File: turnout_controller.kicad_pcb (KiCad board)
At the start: 2 copper layers, 25.4 x 12.7 mm, 31 parts, among them J1 DCC_A, J2 DCC_B, J3 PROG, J4 MOT_CNTL, J5 MOT_POWER, J6 MOT_GND, J7 LED_1, J8 LED_2, SW1 SW_Push, SW2 SW_Push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

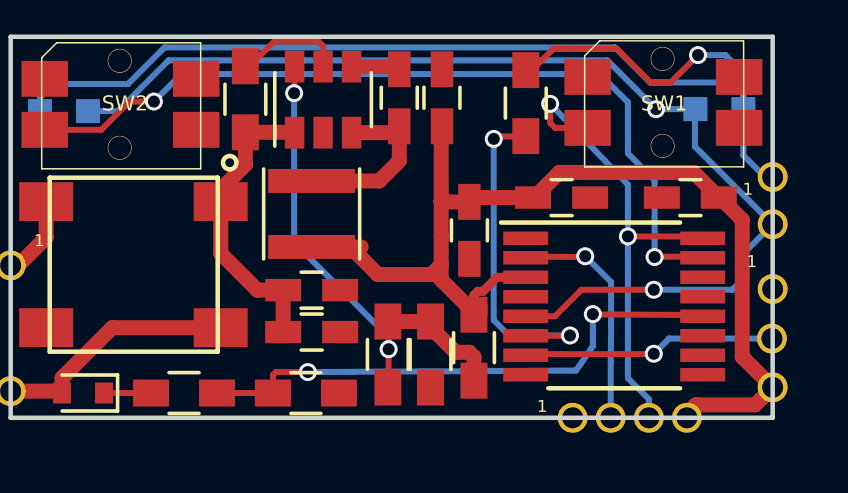
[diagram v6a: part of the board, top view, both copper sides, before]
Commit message: DRC fixes (via moved, trace modified. No GND connections.
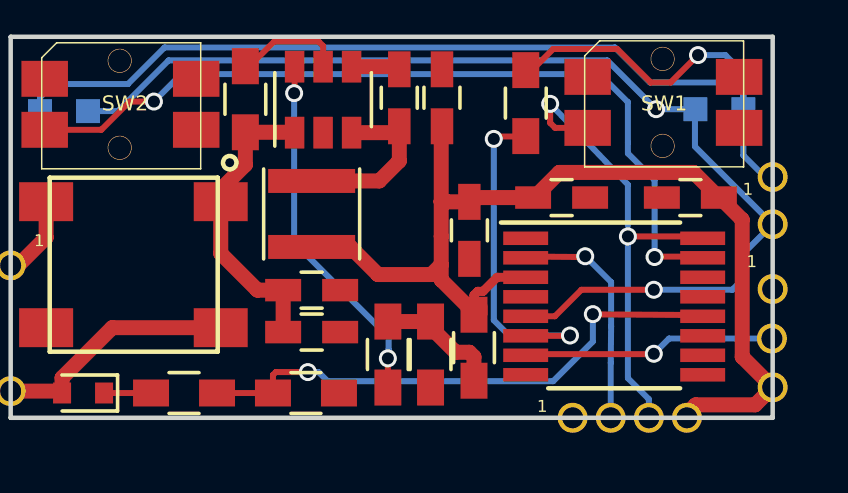
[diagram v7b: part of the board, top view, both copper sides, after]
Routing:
- net 5V: track 37.9 -> 36.3 mm
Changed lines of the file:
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@@
     (thickness 1.6)
     (drawings 10)
-    (tracks 189)
+    (tracks 192)
     (zones 0)
     (modules 31)
@@
   )
   (setup
-    (last_trace_width 0.5)
+    (last_trace_width 0.2)
     (user_trace_width 0.2)
     (user_trace_width 0.3)
@@
   (segment (start 154.1272 81.5848) (end 153.035 80.4926) (width 0.5) (layer F.Cu) (net 5))
   (segment (start 153.035 80.4926) (end 153.035 79.9846) (width 0.5) (layer F.Cu) (net 5))
-  (segment (start 148.717 79.3955) (end 150.368 79.3955) (width 0.5) (layer F.Cu) (net 5))
   (segment (start 148.717 79.3955) (end 150.0075 79.3955) (width 0.5) (layer F.Cu) (net 5))
   (segment (start 150.0075 79.3955) (end 150.9268 80.3148) (width 0.5) (layer F.Cu) (net 5))
@@
   (segment (start 148.9456 72.5424) (end 149.098 72.6948) (width 0.2) (layer F.Cu) (net 11))
   (segment (start 149.098 72.6948) (end 149.098 73.3855) (width 0.2) (layer F.Cu) (net 11))
+  (segment (start 148.59 83.566) (end 148.9456 83.566) (width 0.2) (layer B.Cu) (net 12))
+  (segment (start 147.4265 83.6627) (end 147.5232 83.566) (width 0.2) (layer F.Cu) (net 12))
+  (segment (start 147.5232 83.566) (end 148.59 83.566) (width 0.2) (layer F.Cu) (net 12))
+  (via (at 148.59 83.566) (size 0.6) (drill 0.4) (layers F.Cu B.Cu) (net 12))
   (segment (start 147.4265 84.2645) (end 147.4265 83.6627) (width 0.2) (layer F.Cu) (net 12))
-  (segment (start 157.5308 83.5152) (end 158.0896 82.7024) (width 0.2) (layer B.Cu) (net 12))
-  (segment (start 158.0896 82.7024) (end 158.0896 81.6356) (width 0.2) (layer B.Cu) (net 12))
-  (via (at 148.59 83.566) (size 0.6) (drill 0.4) (layers F.Cu B.Cu) (net 12))
+  (segment (start 156.7688 83.8708) (end 158.0896 82.55) (width 0.2) (layer B.Cu) (net 12))
+  (segment (start 149.2504 83.8708) (end 156.7688 83.8708) (width 0.2) (layer B.Cu) (net 12))
+  (segment (start 148.9456 83.566) (end 149.2504 83.8708) (width 0.2) (layer B.Cu) (net 12))
+  (segment (start 158.0896 82.55) (end 158.0896 81.6356) (width 0.2) (layer B.Cu) (net 12))
+  (segment (start 158.0971 81.6431) (end 162.1445 81.6685) (width 0.2) (layer F.Cu) (net 12))
+  (segment (start 158.0896 81.6356) (end 158.0971 81.6431) (width 0.2) (layer F.Cu) (net 12))
   (via (at 158.0896 81.6356) (size 0.6) (drill 0.4) (layers F.Cu B.Cu) (net 12))
-  (segment (start 158.0896 81.6356) (end 158.0971 81.6431) (width 0.2) (layer F.Cu) (net 12))
-  (segment (start 158.0971 81.6431) (end 162.1445 81.6685) (width 0.2) (layer F.Cu) (net 12))
-  (segment (start 148.59 83.566) (end 157.5308 83.5152) (width 0.2) (layer B.Cu) (net 12))
-  (segment (start 147.5232 83.566) (end 148.59 83.566) (width 0.2) (layer F.Cu) (net 12))
-  (segment (start 147.4265 83.6627) (end 147.5232 83.566) (width 0.2) (layer F.Cu) (net 12))
   (segment (start 145.5625 84.2645) (end 147.4265 84.2645) (width 0.2) (layer F.Cu) (net 12))
+  (segment (start 151.257 84.0818) (end 151.257 83.1088) (width 0.2) (layer F.Cu) (net 13))
+  (segment (start 151.2824 82.3976) (end 148.1328 79.248) (width 0.2) (layer B.Cu) (net 13))
+  (segment (start 148.1328 79.248) (end 148.1328 74.2696) (width 0.2) (layer B.Cu) (net 13))
   (segment (start 151.2824 82.804) (end 151.2824 82.3976) (width 0.2) (layer B.Cu) (net 13))
-  (via (at 151.2824 82.804) (size 0.6) (drill 0.4) (layers F.Cu B.Cu) (net 13))
-  (segment (start 151.2824 83.8532) (end 151.2824 82.804) (width 0.2) (layer F.Cu) (net 13))
-  (segment (start 148.1328 79.248) (end 148.1328 74.2696) (width 0.2) (layer B.Cu) (net 13))
-  (segment (start 151.2824 82.3976) (end 148.1328 79.248) (width 0.2) (layer B.Cu) (net 13))
+  (segment (start 151.2824 83.0834) (end 151.2824 82.804) (width 0.2) (layer B.Cu) (net 13))
+  (segment (start 151.257 83.1088) (end 151.2824 83.0834) (width 0.2) (layer B.Cu) (net 13))
+  (via (at 151.257 83.1088) (size 0.6) (drill 0.4) (layers F.Cu B.Cu) (net 13))
   (segment (start 148.1328 74.4728) (end 148.1328 74.2696) (width 0.2) (layer B.Cu) (net 13))
   (segment (start 148.148 74.2544) (end 148.148 73.3855) (width 0.2) (layer F.Cu) (net 13))

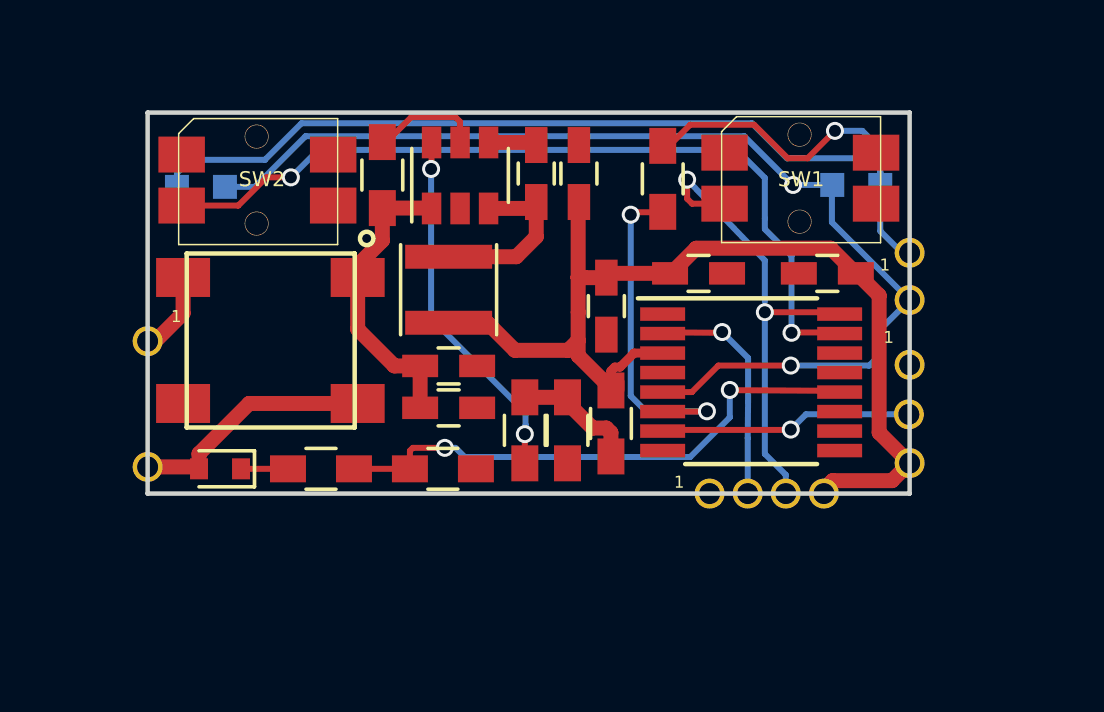
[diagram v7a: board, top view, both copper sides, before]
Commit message: Updated PCB layout w/fill zones. Requires mouting hole and pads
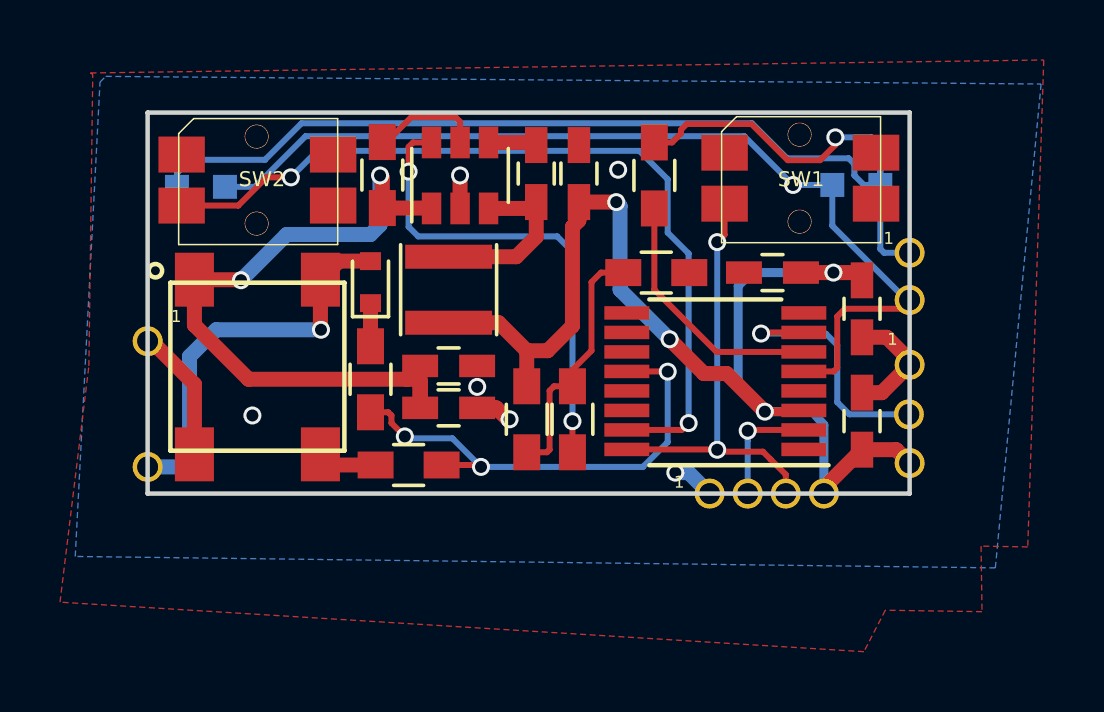
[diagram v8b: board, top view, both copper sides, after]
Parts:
- moved C6 8.52 mm to (162.5, 78.9)
- moved D1 7.99 mm to (146.1, 78.0), turned to 90 degrees
- moved R5 6.03 mm to (155.6, 77.7), turned to 0 degrees
- moved C7 5.06 mm to (162.5, 82.7), turned to 90 degrees
- moved R2 3.41 mm to (146.1, 81.3), turned to 270 degrees
- moved D2 2.97 mm to (144.8, 81.7), turned to 0 degrees
- moved R6 2.81 mm to (151.3, 82.6)
- moved C5 2.46 mm to (159.5, 77.7), turned to 0 degrees
- moved R4 1.63 mm to (152.8, 82.6)
- moved U2 1.19 mm to (157.6, 81.3), turned to 180 degrees
- moved R3 1.15 mm to (147.4, 84.1), turned to 180 degrees
- moved R7 0.30 mm to (155.6, 74.5)
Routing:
- net 12V: track 10.0 -> 24.1 mm, vias 0 -> 2
- net GND: track 0.32 -> 9.85 mm, vias 0 -> 6
- net 5V: track 36.3 -> 42.1 mm, vias 0 -> 4
- net /DCC_A: track 8.23 -> 13.3 mm, vias 0 -> 1
- net /LED2: track 36.5 -> 32.1 mm, vias 2 -> 1
- net Net-(R4-Pad2): track 4.48 -> 8.81 mm
- net Net-(R4-Pad1): track 12.6 -> 16.4 mm
- net /SWD_IO: track 7.34 -> 3.98 mm
- net Net-(R7-Pad1): track 11.5 -> 8.55 mm, vias 2 -> 0
- net /DCC_IN: track 18.8 -> 16.2 mm, vias 2 -> 3
- net /KEY_UP: track 17.9 -> 15.6 mm
- net /DCC_B: track 2.76 -> 4.75 mm
- net /LED1: track 38.4 -> 40.0 mm
- net Net-(J4-Pad1): track 8.03 -> 8.87 mm
- added copper zone on B.Cu, net GND
- added copper zone on F.Cu, net GND
